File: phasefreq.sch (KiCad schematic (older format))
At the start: 109 parts, among them J1 Power Input, J2 RF Input, J3 LO Input, J4 VCO Tune, U1 LM337_SOT223, U2 LM337_SOT223, U3 LM317_3PinPackage, U4 LM337_SOT223, U5 ADCMP564, U6 AD9901, U7 LM4040DBZ-3, U8 AD8676, U9 AD8676

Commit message: Fixed bugs found in revA1 fab
Fixed U5 wiring flip, R23 value so U7 has enough current, added jumpers to flip input to differential amplifier U9B, made bias to U9B bipolar
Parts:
- removed C14, C15: 47u, Capacitor_Tantalum_SMD:CP_EIA-7343-43_Kemet-X, symbol Device:CP_Small
- removed C18, C19, C5, C6: 100n, Capacitor_SMD:C_0603_1608Metric, symbol Device:C_Small
- removed FB1, FB2: BLM31PG601SN1L, Inductor_SMD:L_1206_3216Metric, symbol Device:Ferrite_Bead_Small
- removed R1: 560, Resistor_SMD:R_0603_1608Metric, symbol Device:R_Small
- removed R11, R12: 5R0, Resistor_SMD:R_0603_1608Metric, symbol Device:R_Small
- removed R2: 330, Resistor_SMD:R_0603_1608Metric, symbol Device:R_Small
- removed R3: 470, Resistor_SMD:R_0603_1608Metric, symbol Device:R_Small
- removed R33: NC, Resistor_SMD:R_0603_1608Metric, symbol Device:R_Small
- removed R34: 0R0, Resistor_SMD:R_0603_1608Metric, symbol Device:R_Small
- removed R4: 150, Resistor_SMD:R_0603_1608Metric, symbol Device:R_Small
- removed U1, U2: LM337_SOT223, Package_TO_SOT_SMD:SOT-223-3_TabPin2, symbol Regulator_Linear:LM337_SOT223
- added C?: DNP, Capacitor_SMD:C_0603_1608Metric, symbol Device:C_Small
- added C?: 100n, Capacitor_SMD:C_0603_1608Metric, symbol Device:C_Small
- added JP?: Diff+, symbol Jumper:Jumper_3_Bridged12
- added JP?: Diff-, symbol Jumper:Jumper_3_Bridged12
- added R?: 0R0, Resistor_SMD:R_0603_1608Metric, symbol Device:R_Small
- added R?: DNP, Resistor_SMD:R_0603_1608Metric, symbol Device:R_Small
- R23: value 12K1 -> 499R
- R30: value 0R0 -> 1K
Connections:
- net labels removed: VCO_TUNE
- wire segments 338 -> 304
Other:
- note added: "Bipolar supply and ground\n"
- note removed: "Analog bipolar supply and ground\n"
- note removed: "ECL supply, termination, and digital ground"
- note removed: "Necessary revisions:\n* Power to U5, swapped rails (check cap polarization)\n* R23 value to ensure sufficient operating current to LM4040\n"
- moved on the sheet: C1, C2, C3, C31, C32, C4, C40, C41, C42, C43, C44, C45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

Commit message: Cleaned up power, regularized pot values
Switched all power references to single bipolar supply, consolidated to a single ground, and set all pot values to be the same (constrained by R_hys on comparators)
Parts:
- RV1, RV4, RV5: value 10K -> 50K
- gave numbers to parts that had none: 6
- renumbered C12 to C10, C13 to C11, C16 to C12, C17 to C13, C20 to C14, C21 to C15, C22 to C16, C23 to C17, C24 to C18, C25 to C19, C26 to C20, C31 to C21, C32 to C22, C27 to C23, C28 to C24, C29 to C25, C30 to C26, C33 to C27, C34 to C28, C35 to C29, C36 to C30, C37 to C31, C38 to C32, C40 to C33, C39 to C34, C43 to C36, C41 to C37, C42 to C38, C44 to C39, C45 to C40, C46 to C42, C47 to C43, C48 to C44, C49 to C45, C50 to C46, C51 to C47, C52 to C48, C53 to C49, C7 to C5, C8 to C6, C9 to C7, C10 to C8, C11 to C9, FB3 to FB1, FB4 to FB2, R5 to R1, R16 to R10, R17 to R11, R18 to R12, R19 to R13, R22 to R14, R20 to R15, R21 to R16, R32 to R17, R24 to R18, R23 to R19, R6 to R2, R25 to R20, R26 to R23, R27 to R24, R28 to R25, R29 to R26, R30 to R27, R31 to R28, R7 to R3, R8 to R4, R9 to R5, R10 to R6, R13 to R7, R14 to R8, R15 to R9, U3 to U1, U4 to U2, U5 to U3, U6 to U4, U7 to U5, U8 to U6, U9 to U7
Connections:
- net labels added: VCC, VEE
- net labels removed: +5VA, -5V, -5VA, GNDD

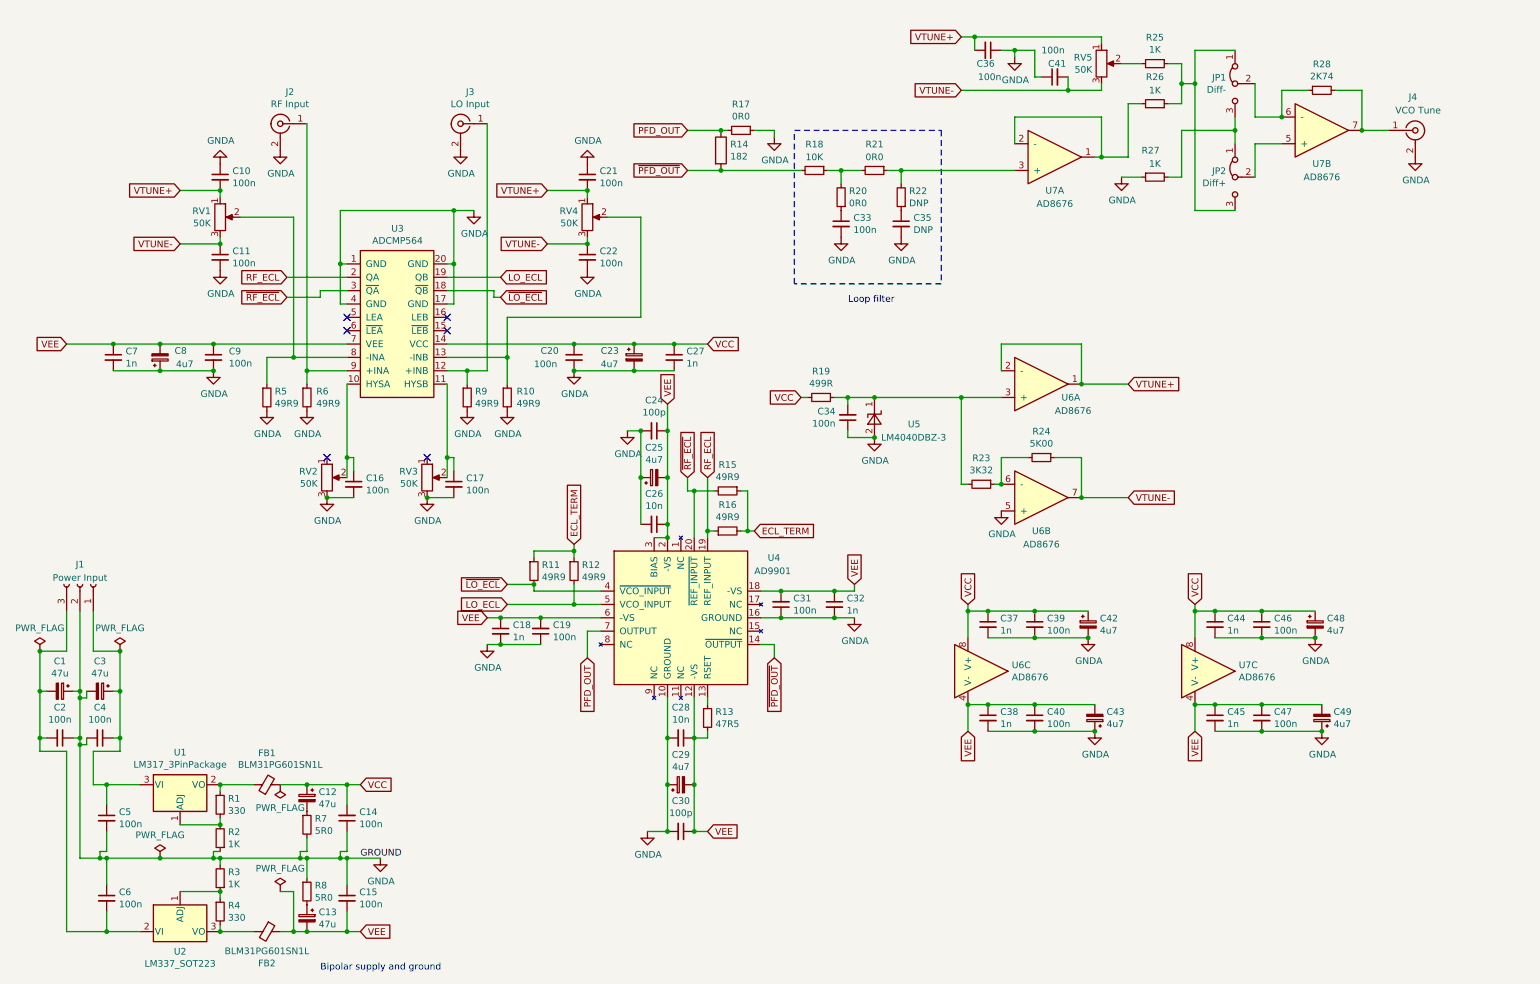
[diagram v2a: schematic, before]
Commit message: switch power from labels to proper power port
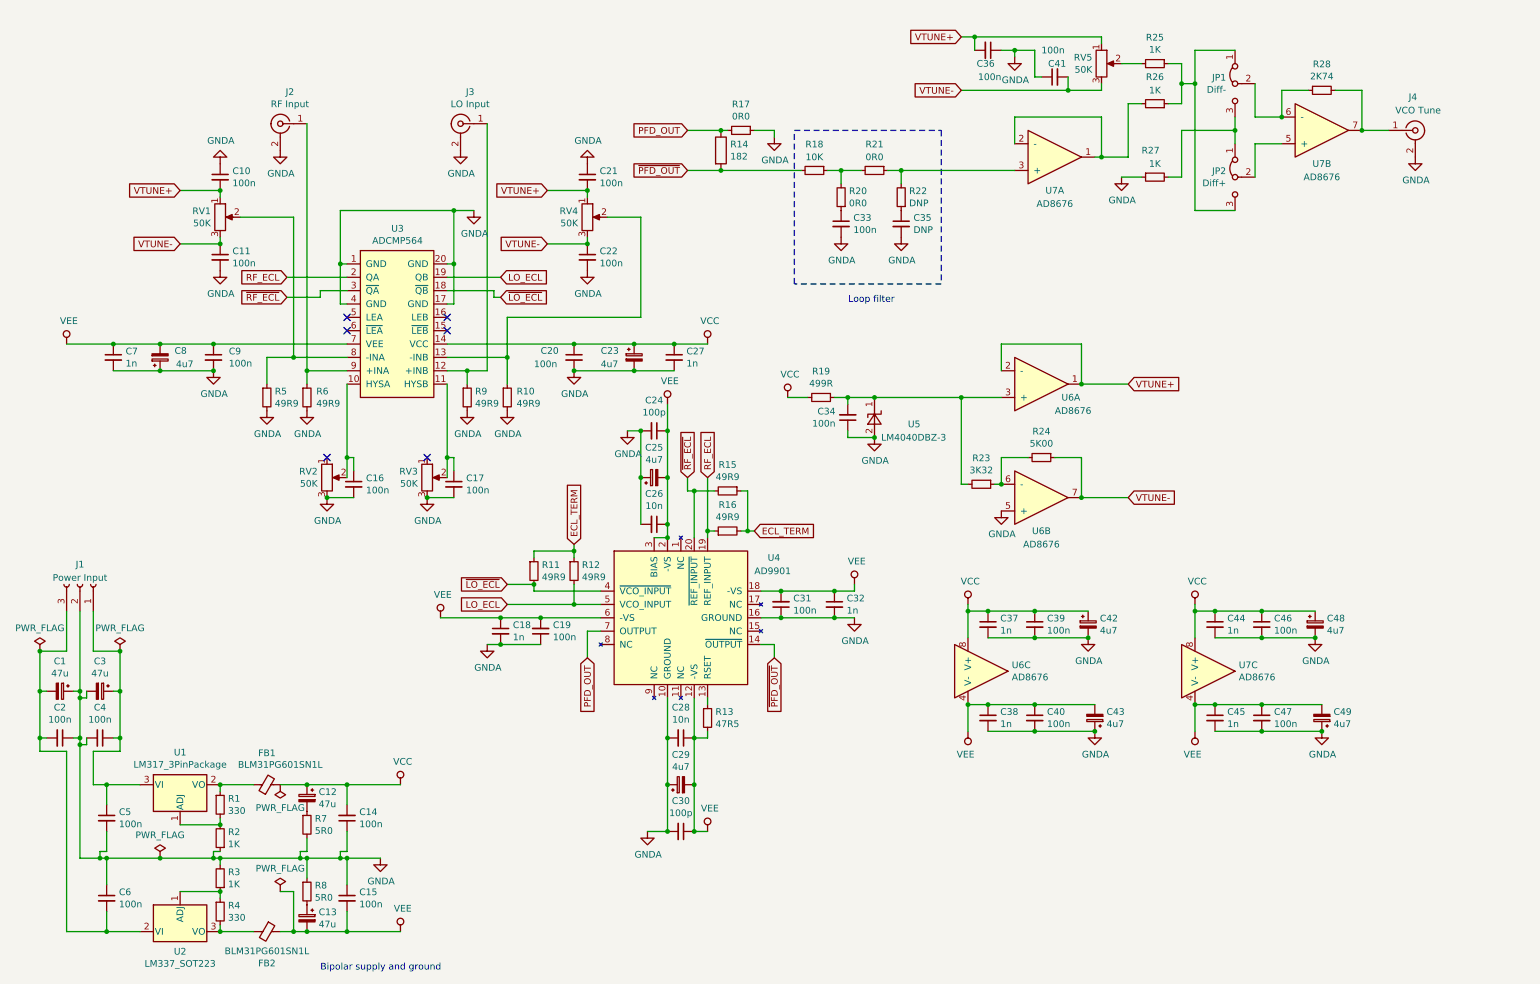
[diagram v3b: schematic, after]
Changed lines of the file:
@@
 	1    0    0    -1
 $EndComp
-Text GLabel 5300 3500 1    50   Input ~ 0
-VEE
 $Comp
 L Device:C_Small C32
@@
 	1    0    0    -1
 $EndComp
-Text GLabel 6700 4850 1    50   Input ~ 0
-VEE
 $Comp
 L Device:C_Small C28
@@
 	1    0    0    -1
 $EndComp
-Text GLabel 5600 6700 2    50   Input ~ 0
-VEE
 $Comp
 L Device:C_Small C19
@@
 	-1   0    0    1
 $EndComp
-Text GLabel 3950 5100 0    50   Input ~ 0
-VEE
 Text GLabel 5450 1450 0    50   Input ~ 0
 PFD_OUT
@@
 	9400 5750 9750 5750
 Connection ~ 9750 5750
-Text GLabel 9250 5000 1    50   Input ~ 0
-VCC
-Text GLabel 9250 5950 3    50   Input ~ 0
-VEE
 $Comp
 L Device:R_Small R28
@@
 Wire Wire Line
 	9250 5050 9250 5000
-Text GLabel 5600 3050 2    50   Input ~ 0
-VCC
-Text GLabel 800  3050 0    50   Input ~ 0
-VEE
 Connection ~ 5050 3050
 $Comp
@@
 Bipolar supply and ground\n
 Connection ~ 2900 7450
-Wire Wire Line
-	3000 7450 2900 7450
 Connection ~ 2600 7450
 Wire Wire Line
@@
 	2900 6900 3150 6900
 Connection ~ 2900 6900
-Wire Wire Line
-	2900 6350 3000 6350
 Connection ~ 2900 6350
 Wire Wire Line
@@
 Wire Wire Line
 	2600 6900 2850 6900
-Text GLabel 3000 7450 2    50   Input ~ 0
-VEE
-Text GLabel 3000 6350 2    50   Input ~ 0
-VCC
 $Comp
 L power:GNDA #PWR08
@@
 Connection ~ 4050 5100
 Wire Wire Line
-	4050 5100 3950 5100
-Wire Wire Line
 	4350 5100 4050 5100
 Wire Wire Line
@@
 Wire Wire Line
 	1100 6350 1350 6350
-Text GLabel 6300 3450 0    50   Input ~ 0
-VCC
 $Comp
 L power:GNDA #PWR023
@@
 Wire Wire Line
 	7550 5750 7550 5950
-Text GLabel 7550 5000 1    50   Input ~ 0
-VCC
-Text GLabel 7550 5950 3    50   Input ~ 0
-VEE
 Wire Wire Line
 	7550 5050 7550 5000
@@
 	6850 3450 7500 3450
 Wire Wire Line
-	6300 3450 6350 3450
-Wire Wire Line
 	7500 3450 7800 3450
 Connection ~ 7500 3450
@@
 	1    0    0    -1
 $EndComp
-Text Label 3000 6900 0    50   ~ 0
-GROUND
 Wire Wire Line
 	5950 1450 6100 1450
@@
 	1    0    0    -1
 $EndComp
+$Comp
+L power:VCC #PWR?
+U 1 1 5DCECB37
+P 3300 6350
+F 0 "#PWR?" H 3300 6200 50  0001 C CNN
+F 1 "VCC" H 3317 6523 50  0000 C CNN
+F 2 "" H 3300 6350 50  0001 C CNN
+F 3 "" H 3300 6350 50  0001 C CNN
+	1    3300 6350
+	1    0    0    -1
+$EndComp
+$Comp
+L power:VEE #PWR?
+U 1 1 5DCED911
+P 3300 7450
+F 0 "#PWR?" H 3300 7300 50  0001 C CNN
+F 1 "VEE" H 3317 7623 50  0000 C CNN
+F 2 "" H 3300 7450 50  0001 C CNN
+F 3 "" H 3300 7450 50  0001 C CNN
+	1    3300 7450
+	1    0    0    -1
+$EndComp
+Wire Wire Line
+	2900 6350 3300 6350
+Wire Wire Line
+	2900 7450 3300 7450
+$Comp
+L power:VEE #PWR?
+U 1 1 5DD259BF
+P 800 3050
+F 0 "#PWR?" H 800 2900 50  0001 C CNN
+F 1 "VEE" H 817 3223 50  0000 C CNN
+F 2 "" H 800 3050 50  0001 C CNN
+F 3 "" H 800 3050 50  0001 C CNN
+	1    800  3050
+	1    0    0    -1
+$EndComp
+$Comp
+L power:VCC #PWR?
+U 1 1 5DD27236
+P 5600 3050
+F 0 "#PWR?" H 5600 2900 50  0001 C CNN
+F 1 "VCC" H 5617 3223 50  0000 C CNN
+F 2 "" H 5600 3050 50  0001 C CNN
+F 3 "" H 5600 3050 50  0001 C CNN
+	1    5600 3050
+	1    0    0    -1
+$EndComp
+$Comp
+L power:VEE #PWR?
+U 1 1 5DD2815B
+P 3600 5100
+F 0 "#PWR?" H 3600 4950 50  0001 C CNN
+F 1 "VEE" H 3617 5273 50  0000 C CNN
+F 2 "" H 3600 5100 50  0001 C CNN
+F 3 "" H 3600 5100 50  0001 C CNN
+	1    3600 5100
+	1    0    0    -1
+$EndComp
+$Comp
+L power:VEE #PWR?
+U 1 1 5DD28462
+P 6700 4850
+F 0 "#PWR?" H 6700 4700 50  0001 C CNN
+F 1 "VEE" H 6717 5023 50  0000 C CNN
+F 2 "" H 6700 4850 50  0001 C CNN
+F 3 "" H 6700 4850 50  0001 C CNN
+	1    6700 4850
+	1    0    0    -1
+$EndComp
+$Comp
+L power:VEE #PWR?
+U 1 1 5DD291AA
+P 5300 3500
+F 0 "#PWR?" H 5300 3350 50  0001 C CNN
+F 1 "VEE" H 5317 3673 50  0000 C CNN
+F 2 "" H 5300 3500 50  0001 C CNN
+F 3 "" H 5300 3500 50  0001 C CNN
+	1    5300 3500
+	1    0    0    -1
+$EndComp
+$Comp
+L power:VEE #PWR?
+U 1 1 5DD2A9C4
+P 5600 6700
+F 0 "#PWR?" H 5600 6550 50  0001 C CNN
+F 1 "VEE" H 5617 6873 50  0000 C CNN
+F 2 "" H 5600 6700 50  0001 C CNN
+F 3 "" H 5600 6700 50  0001 C CNN
+	1    5600 6700
+	1    0    0    -1
+$EndComp
+Wire Wire Line
+	3600 5100 4050 5100
+$Comp
+L power:VCC #PWR?
+U 1 1 5DD46C33
+P 7550 5000
+F 0 "#PWR?" H 7550 4850 50  0001 C CNN
+F 1 "VCC" H 7567 5173 50  0000 C CNN
+F 2 "" H 7550 5000 50  0001 C CNN
+F 3 "" H 7550 5000 50  0001 C CNN
+	1    7550 5000
+	1    0    0    -1
+$EndComp
+$Comp
+L power:VCC #PWR?
+U 1 1 5DD4709C
+P 9250 5000
+F 0 "#PWR?" H 9250 4850 50  0001 C CNN
+F 1 "VCC" H 9267 5173 50  0000 C CNN
+F 2 "" H 9250 5000 50  0001 C CNN
+F 3 "" H 9250 5000 50  0001 C CNN
+	1    9250 5000
+	1    0    0    -1
+$EndComp
+$Comp
+L power:VEE #PWR?
+U 1 1 5DD49594
+P 7550 5950
+F 0 "#PWR?" H 7550 5800 50  0001 C CNN
+F 1 "VEE" H 7568 6123 50  0000 C CNN
+F 2 "" H 7550 5950 50  0001 C CNN
+F 3 "" H 7550 5950 50  0001 C CNN
+	1    7550 5950
+	-1   0    0    1
+$EndComp
+$Comp
+L power:VEE #PWR?
+U 1 1 5DD4A69C
+P 9250 5950
+F 0 "#PWR?" H 9250 5800 50  0001 C CNN
+F 1 "VEE" H 9268 6123 50  0000 C CNN
+F 2 "" H 9250 5950 50  0001 C CNN
+F 3 "" H 9250 5950 50  0001 C CNN
+	1    9250 5950
+	-1   0    0    1
+$EndComp
+$Comp
+L power:VCC #PWR?
+U 1 1 5DD4AB86
+P 6200 3450
+F 0 "#PWR?" H 6200 3300 50  0001 C CNN
+F 1 "VCC" H 6217 3623 50  0000 C CNN
+F 2 "" H 6200 3450 50  0001 C CNN
+F 3 "" H 6200 3450 50  0001 C CNN
+	1    6200 3450
+	1    0    0    -1
+$EndComp
+Wire Wire Line
+	6200 3450 6350 3450
 $EndSCHEMATC

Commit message: Added TVS diode array to comparator input
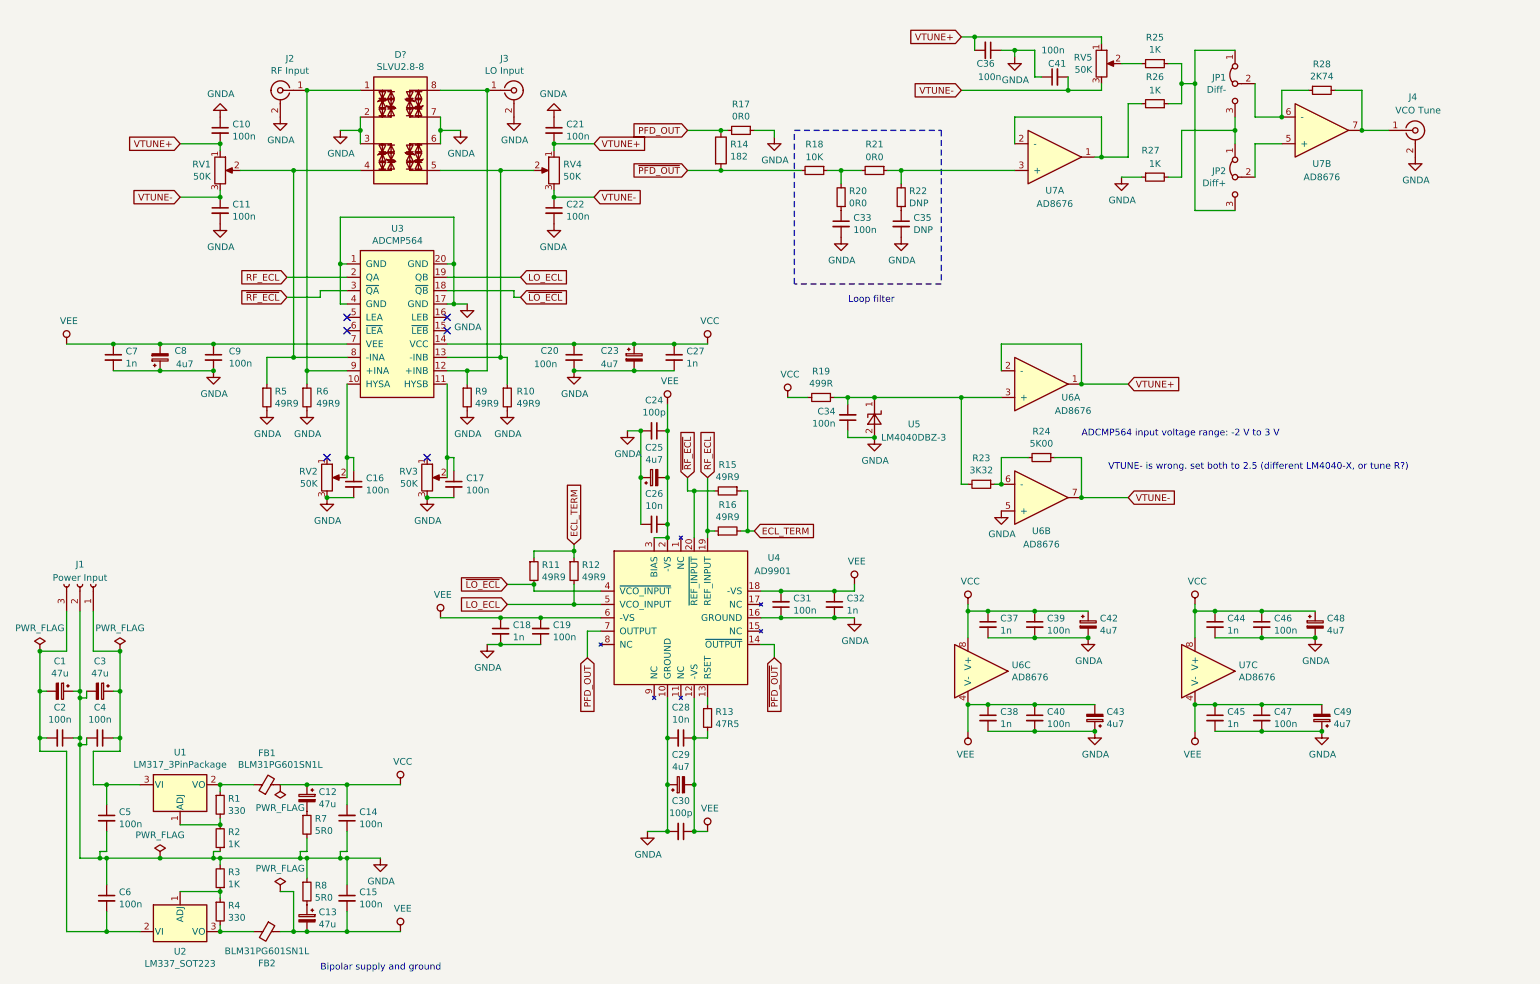
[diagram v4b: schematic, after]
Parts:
- added D?: SLVU2.8-8, Package_SO:SOIC-8_3.9x4.9mm_P1.27mm, symbol grav:SLVU2.8-8
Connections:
- net GNDA: now also D?.2 (TVS2), D?.3 (TVS1), D?.6 (TVS2), D?.7 (TVS1)
- net at J2.1 (In), R6.1, U3.9 (+INA): now also D?.1 (TVS1)
- net at R10.1, RV4.2, U3.13 (-INB): now also D?.5 (TVS1)
- net at J3.1 (In), R9.1, U3.12 (+INB): now also D?.8 (TVS2)
- net at R5.1, RV1.2, U3.8 (-INA): now also D?.4 (TVS2)
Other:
- note added: "ADCMP564 input voltage range: -2 V to 3 V"
- note added: "VTUNE- is wrong. set both to 2.5 (different LM4040-X, or tune R?)"
- moved on the sheet: C10, C11, C21, C22, J2, J3, RV1, RV4
